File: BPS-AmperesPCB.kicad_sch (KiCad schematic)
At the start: 18 parts, among them J1 ShuntConn, U1 PeripheralSOM, U2 INA229AIDGSR, U3 AMC1300BDWV, U4 RO-123.3S_HP

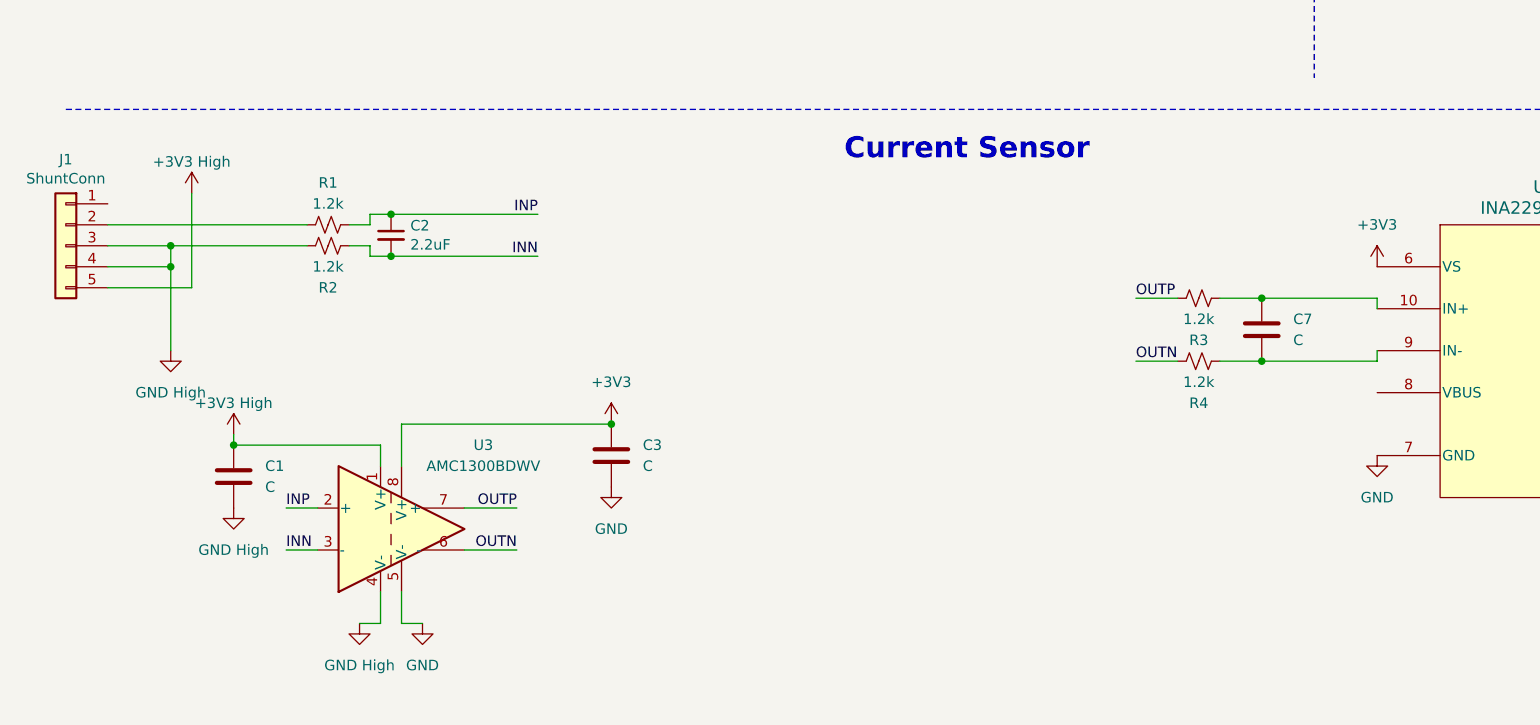
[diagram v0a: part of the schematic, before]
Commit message: Corrections with resistor values and slight components
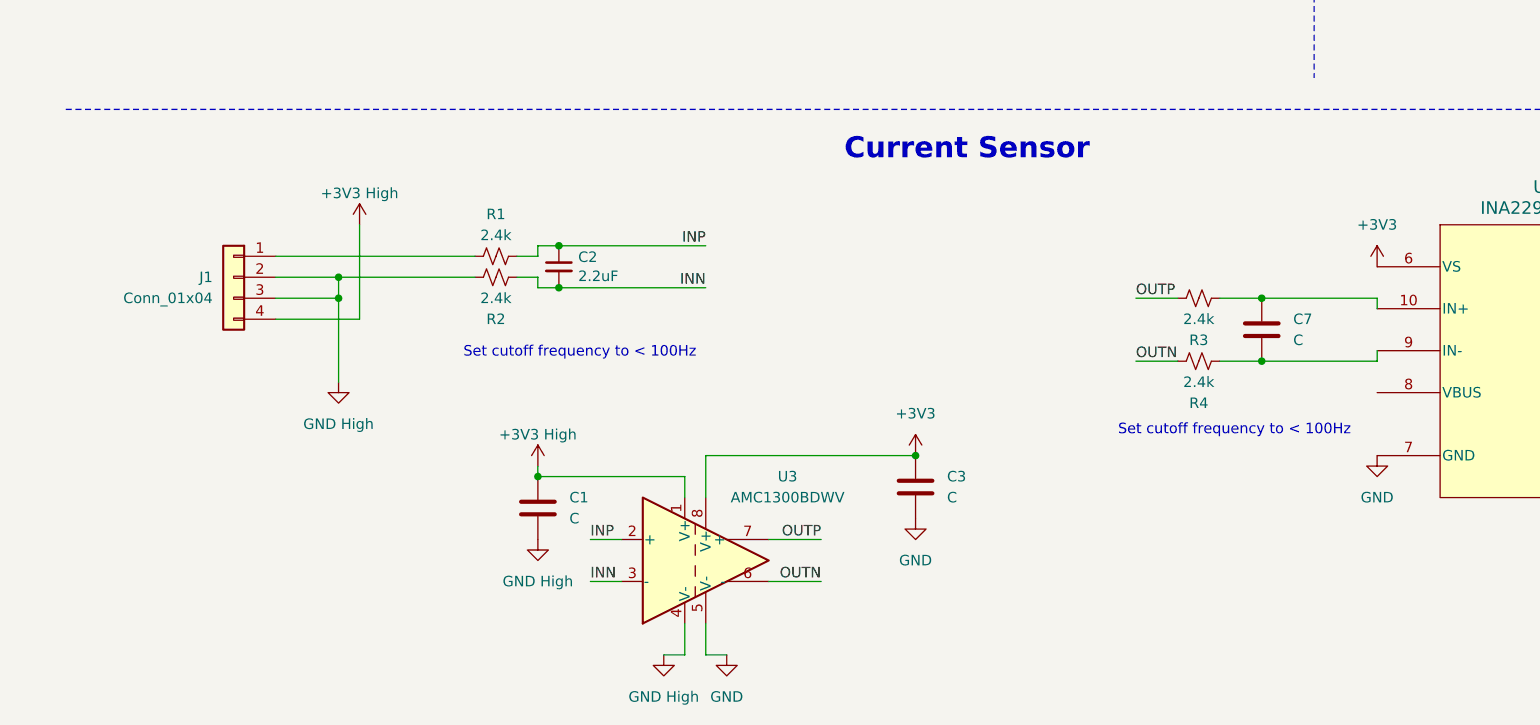
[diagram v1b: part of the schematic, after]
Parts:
- removed J1: ShuntConn, Connector_PinSocket_2.54mm:PinSocket_1x05_P2.54mm_Vertical, symbol Connector_Generic:Conn_01x05
- added J1: Conn_01x04, symbol Connector_Generic:Conn_01x04
- R1, R2, R3, R4: value 1.2k -> 2.4k
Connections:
- net +3V3 High: now also J1.4 (Pin_4)
- net GND High: now also J1.2 (Pin_2), J1.3 (Pin_3)
- net at R1.2: now also J1.1 (Pin_1)
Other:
- note added: "Set cutoff frequency to < 100Hz"
- moved on the sheet: C1, C2, C3, R1, R2, U3

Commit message: done
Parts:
- removed U2: INA229AIDGSR, VSSOP10_DGS_TEX, symbol INA229:INA229AIDGSR
- added C8: 2.2uF, symbol Device:C
- added D2, D3: RBE01VYM6AFHTR, RBE01VYM6AFHTR, symbol usvt-chips:RBE01VYM6AFHTR
- added J2, J3: PeripheralCANConnector, UTSVT_Connectors:Molex_MicroFit3.0_1x4xP3.00mm_PolarizingPeg_Vertical, symbol utsvt-connectors:PeripheralCANConnector
- added R6: 12k, Resistor_SMD:R_0805_2012Metric, symbol Device:R_Small_US
- added R7: 1k, Resistor_SMD:R_0805_2012Metric, symbol Device:R_Small_US
- added R8: 4.8k, Resistor_SMD:R_0805_2012Metric, symbol Device:R_Small_US
- added U2: INA145UA/2K5, D8, symbol usvt-chips:INA145UA_2K5
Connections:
- net +3V3: now also D2.1 (K), U2.7 (V+)
- net GND: now also C8.2, D3.2 (A), R7.2, U2.1 (REF), U2.4 (V-)
- net at C7.1, R3.1: now also U2.2 (V-IN)
- net at C7.2, R4.1: now also U2.3 (V+IN)
- net ADC_In: now reaches U1.20 (PA1(ADC))
- net ADC_In: now also C8.1, R8.1
- new net: R6.2, R7.1, U2.5 (RG)
- new net: D2.2 (A), D3.1 (K), R6.1, R8.2, U2.6 (VO)
